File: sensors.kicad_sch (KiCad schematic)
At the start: 8 parts, among them U1 BNO055

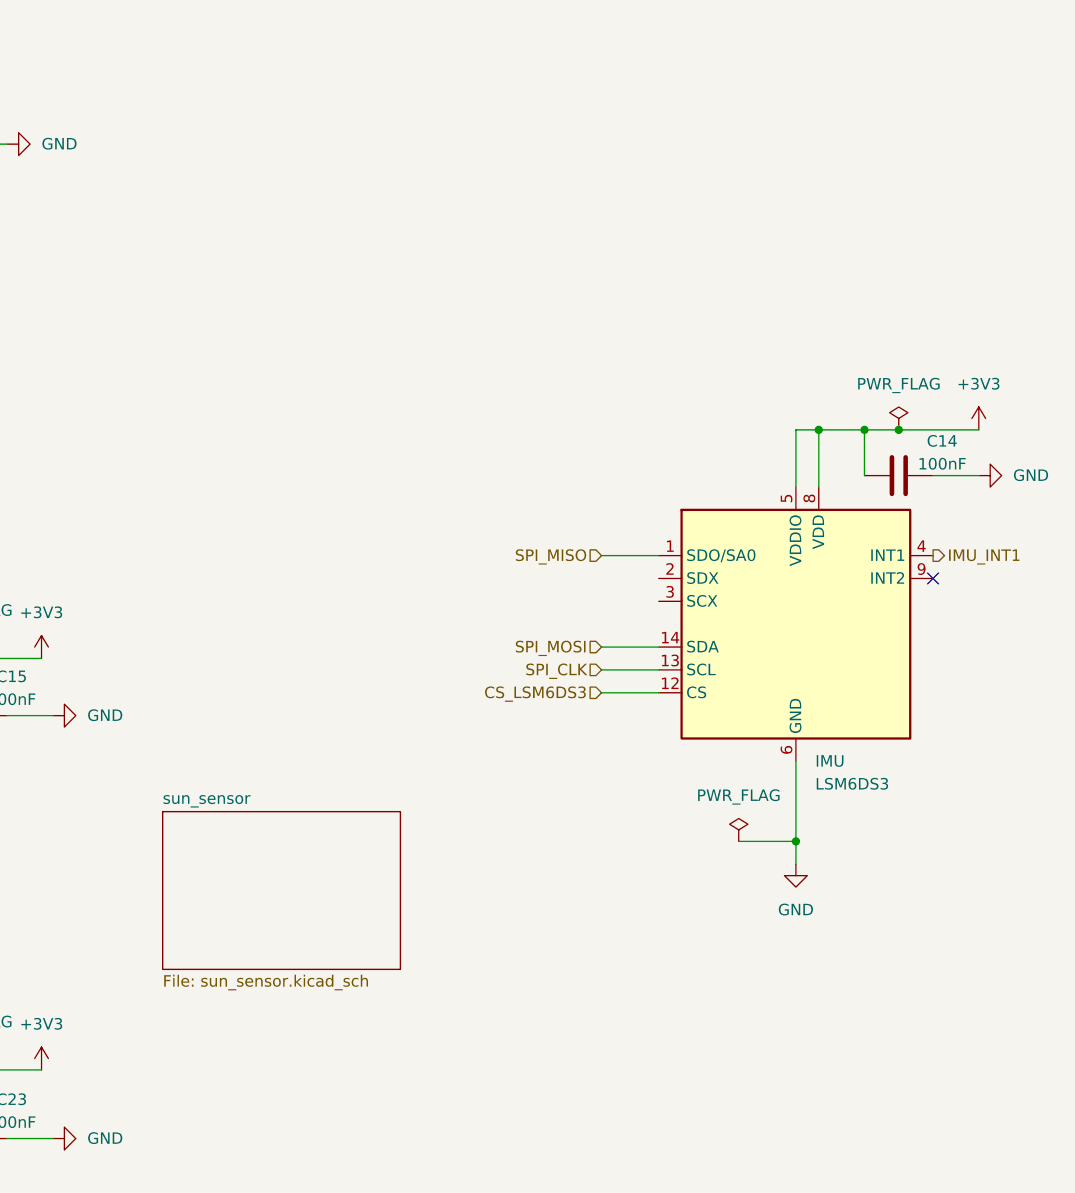
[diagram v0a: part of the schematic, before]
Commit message: Add XYZ photodiodes to sun sensor. Fix hierarchical labels on MCU.
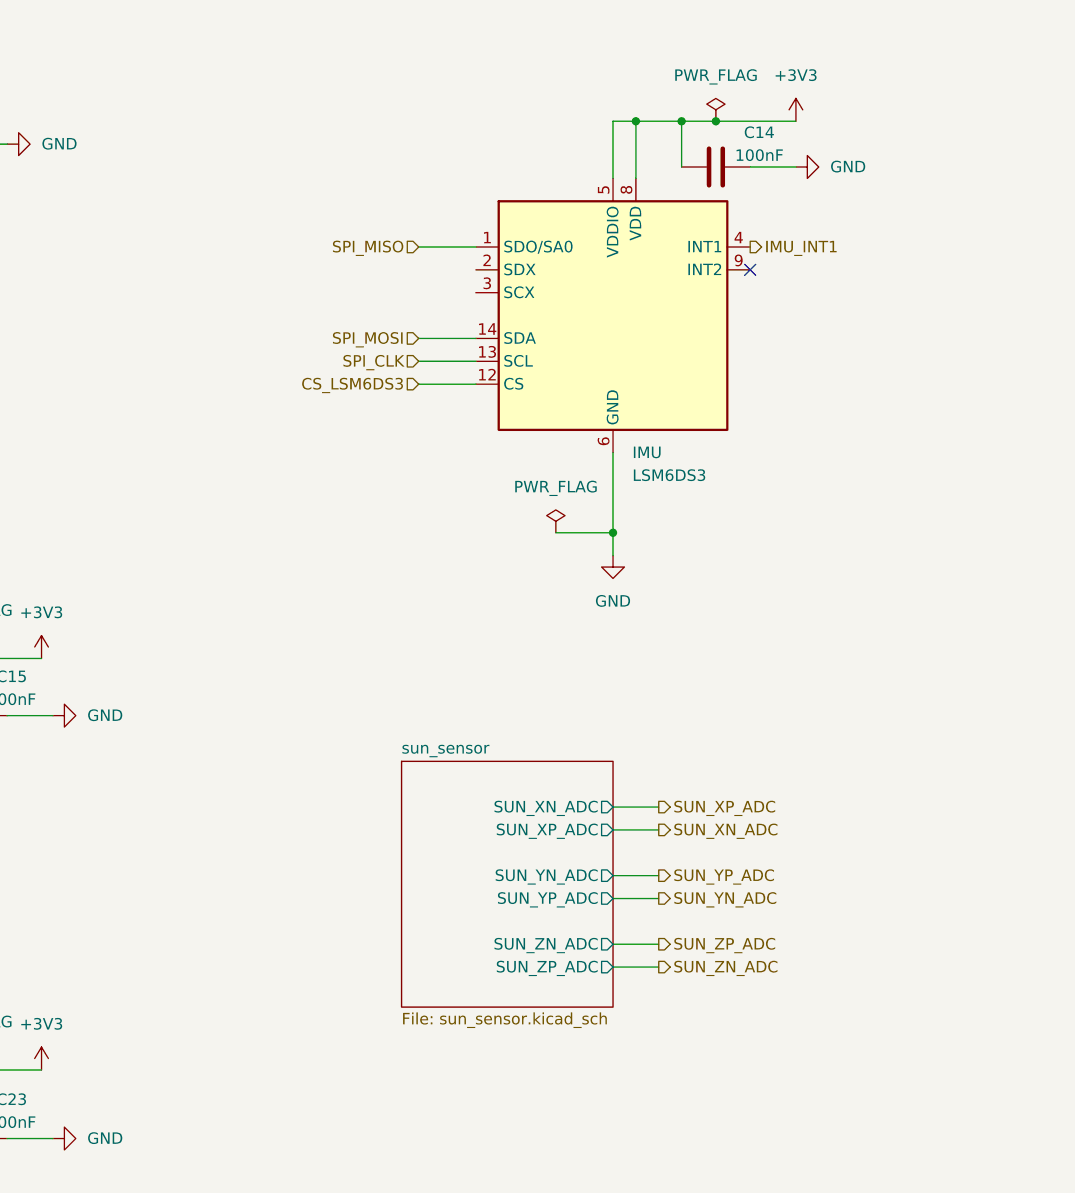
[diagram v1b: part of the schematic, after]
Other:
- sheet sun_sensor ports: added SUN_XN_ADC, SUN_XP_ADC, SUN_YN_ADC, SUN_YP_ADC, SUN_ZN_ADC, SUN_ZP_ADC; removed none
- moved on the sheet: C14, IMU

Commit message: Fix sun sensor axis label mismatch
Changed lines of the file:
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@@
 		)
 	)
-	(hierarchical_label "SUN_ZN_ADC"
+	(hierarchical_label "SUN_YP_ADC"
+		(shape output)
+		(at 205.74 116.84 0)
+		(effects
+			(font
+				(size 1.27 1.27)
+			)
+			(justify left)
+		)
+	)
+	(hierarchical_label "SUN_ZP_ADC"
 		(shape output)
 		(at 205.74 124.46 0)
@@
 		)
 	)
-	(hierarchical_label "SUN_YP_ADC"
-		(shape output)
-		(at 205.74 114.3 0)
-		(effects
-			(font
-				(size 1.27 1.27)
-			)
-			(justify left)
-		)
-	)
 	(hierarchical_label "SPI_CLK"
 		(shape input)
 		(at 39.37 85.09 0)
-		(effects
-			(font
-				(size 1.27 1.27)
-			)
-			(justify left)
-		)
-	)
-	(hierarchical_label "SUN_ZP_ADC"
-		(shape output)
-		(at 205.74 121.92 0)
 		(effects
 			(font
@@
 		)
 	)
+	(hierarchical_label "SUN_YN_ADC"
+		(shape output)
+		(at 205.74 114.3 0)
+		(effects
+			(font
+				(size 1.27 1.27)
+			)
+			(justify left)
+		)
+	)
 	(hierarchical_label "SPI_MISO"
 		(shape input)
@@
 			)
 			(justify right)
-		)
-	)
-	(hierarchical_label "SUN_XN_ADC"
-		(shape output)
-		(at 205.74 109.22 0)
-		(effects
-			(font
-				(size 1.27 1.27)
-			)
-			(justify left)
-		)
-	)
-	(hierarchical_label "SUN_YN_ADC"
-		(shape output)
-		(at 205.74 116.84 0)
-		(effects
-			(font
-				(size 1.27 1.27)
-			)
-			(justify left)
 		)
 	)
@@
 		)
 	)
-	(hierarchical_label "IMU_INT1"
+	(hierarchical_label "SUN_XP_ADC"
 		(shape output)
-		(at 215.9 44.45 0)
+		(at 205.74 109.22 0)
 		(effects
 			(font
@@
 		)
 	)
-	(hierarchical_label "SUN_XP_ADC"
+	(hierarchical_label "SUN_XN_ADC"
 		(shape output)
 		(at 205.74 106.68 0)
 		(effects
 			(font
+				(size 1.27 1.27)
+			)
+			(justify left)
+		)
+	)
+	(hierarchical_label "SUN_ZN_ADC"
+		(shape output)
+		(at 205.74 121.92 0)
+		(effects
+			(font
+				(size 1.27 1.27)
+			)
+			(justify left)
+		)
+	)
+	(hierarchical_label "IMU_INT1"
+		(shape output)
+		(at 215.9 44.45 0)
+		(effects
+			(font
